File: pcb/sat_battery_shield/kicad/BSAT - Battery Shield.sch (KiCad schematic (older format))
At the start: 10 parts, among them P2 POWER, SW2 SAT POWER, U1 TP4056-MODULE, U2 TP4056-MODULE

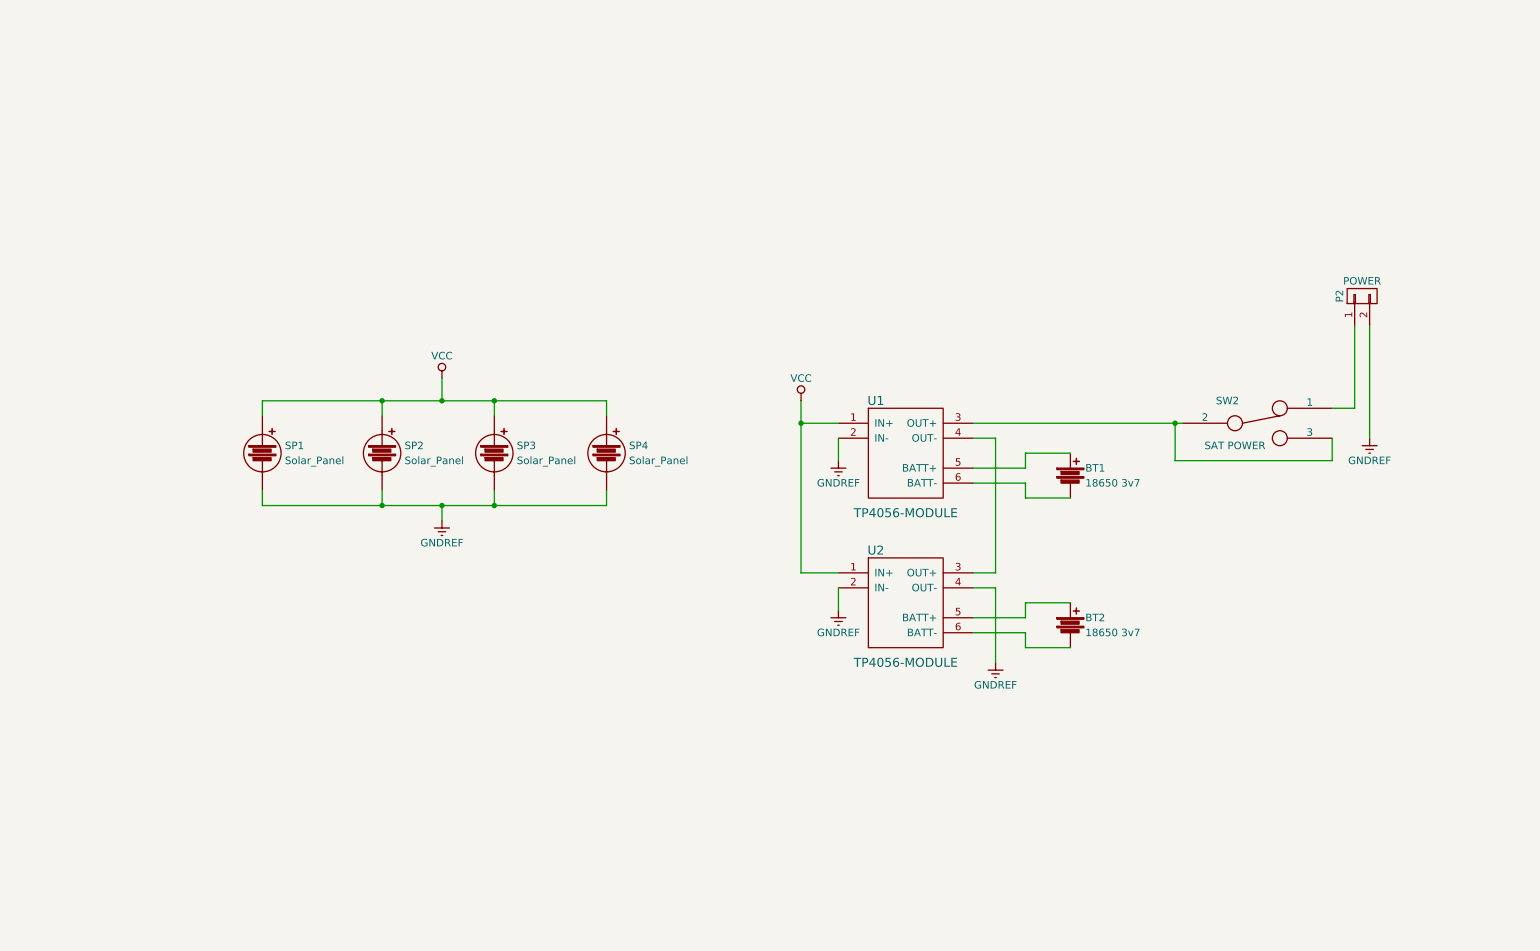
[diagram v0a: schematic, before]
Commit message: feat(battery-shield): Esquema reorganizado y optoacoplador añadido para el enable/disable del cargador.
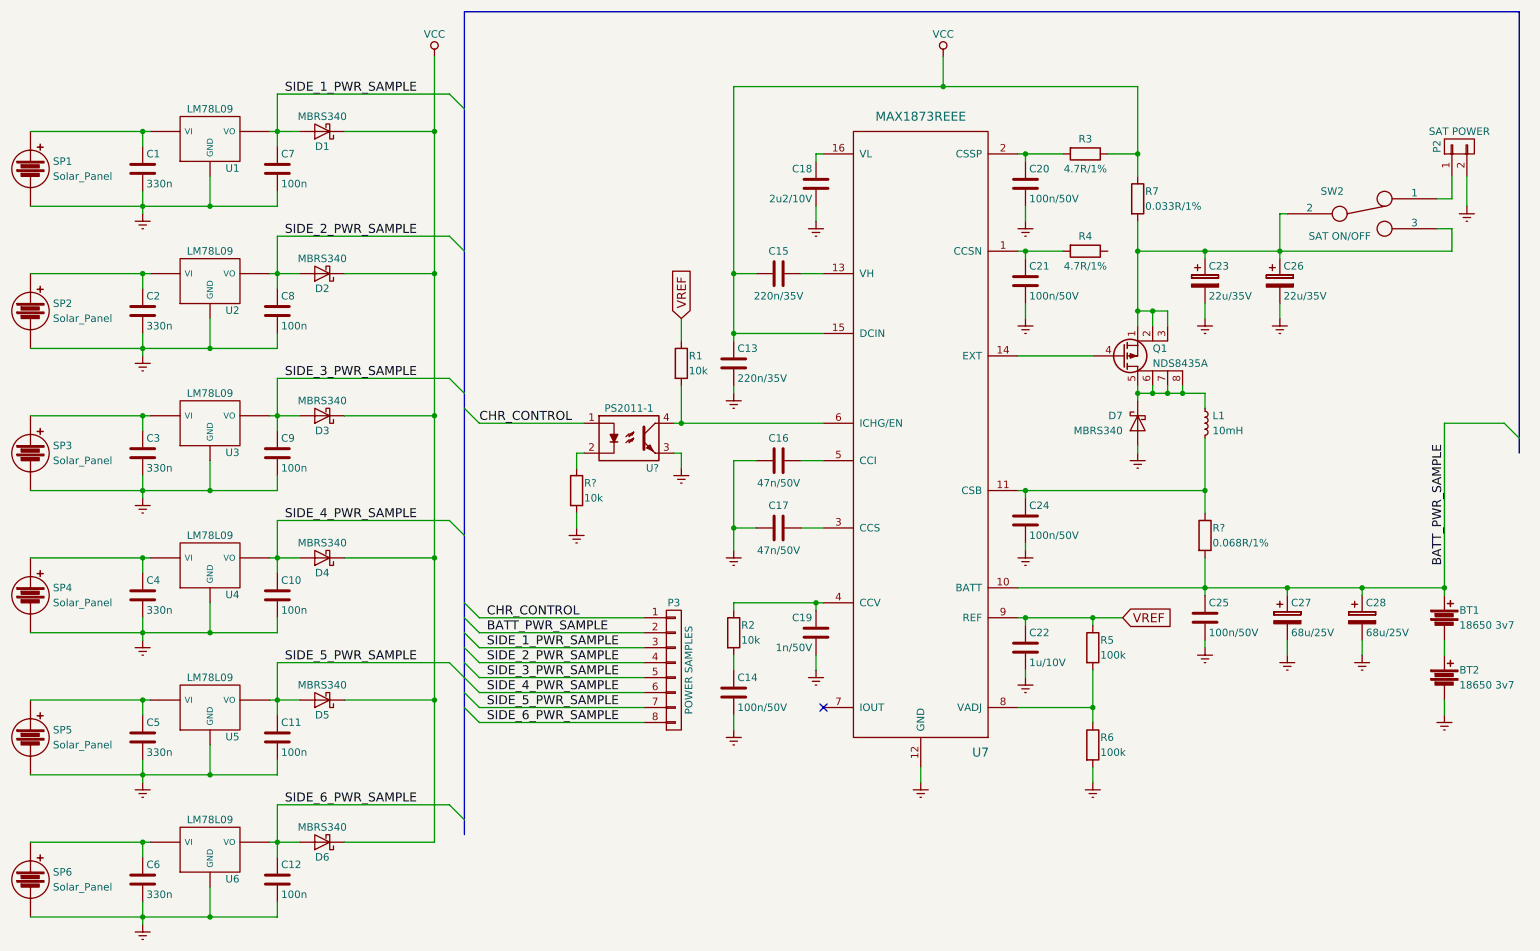
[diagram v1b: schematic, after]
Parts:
- removed U1, U2: TP4056-MODULE, BoscoverySAT:TP4056-MODULE, symbol TP4056-MODULE
- added C1, C2, C3, C4, C5, C6: 330n, symbol C
- added C10, C11, C12, C7, C8, C9: 100n, symbol C
- added C13, C15: 220n/35V, symbol C
- added C14, C20, C21, C24, C25: 100n/50V, symbol C
- added C16, C17: 47n/50V, symbol C
- added C18: 2u2/10V, symbol C
- added C19: 1n/50V, symbol C
- added C22: 1u/10V, symbol C
- added C23, C26: 22u/35V, symbol CP
- added C27, C28: 68u/25V, symbol CP
- added D1, D2, D3, D4, D5, D6, D7: MBRS340, symbol D_Schottky
- added L1: 10mH, symbol L_Small
- added P3: POWER SAMPLES, symbol CONN_01X08
- added Q1: NDS8435A, symbol NDS8435A
- added R1, R2, R?: 10k, symbol R
- added R3, R4: 4.7R/1%, symbol R
- added R5, R6: 100k, symbol R
- added R7: 0.033R/1%, symbol R
- added R?: 0.068R/1%, symbol R
- added SP5, SP6: Solar_Panel, Pin_Headers:Pin_Header_Straight_1x02, symbol Solar_Panel
- added U1, U2, U3, U4, U5, U6: LM78L09, symbol LM78L09
- added U7: MAX1873REEE, symbol MAX1873REEE
- added U?: PS2011-1, symbol PS2011-1
- P2: value POWER -> SAT POWER
- SW2: value SAT POWER -> SAT ON/OFF
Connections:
- net GNDREF: now also BT2.2, C1.2, C10.2, C11.2, C12.2, C13.2, C14.2, C16.1, C17.1, C18.2, C19.2, C2.2, C20.2, C21.2, C22.2, C23.2, C24.2, C25.2, C26.2, C27.2, C28.2, C3.2, C4.2, C5.2, C6.2, C7.2, C8.2, C9.2, D7.2 (A), R6.2, R?.2, SP5.2, SP6.2, U1.GND, U2.GND, U3.GND, U4.GND, U5.GND, U6.GND, U7.12 (GND), U?.3
- net VCC: now also C13.1, C15.1, D1.1 (K), D2.1 (K), D3.1 (K), D4.1 (K), D5.1 (K), D6.1 (K), R3.1, R7.1, U7.15 (DCIN); no longer SP1.1, SP2.1, SP3.1, SP4.1
- net at SW2.2, SW2.3: now also C23.1, C26.1, Q1.1 (S), Q1.2 (S), Q1.3 (S), R7.2
- net BATT_PWR_SAMPLE: now reaches BT1.1
- net BATT_PWR_SAMPLE: now also C25.1, C27.1, C28.1, P3.2 (P2), R?.2, U7.10 (BATT)
- net at BT1.2: now also BT2.1
- new net: C1.1, SP1.1, U1.VI
- new net: C21.1, R4.2, U7.1 (CCSN)
- new net: C24.1, L1.2, R?.1, U7.11 (CSB)
- new net: C15.2, U7.13 (VH)
- new net: Q1.4 (G), U7.14 (EXT)
- new net: C18.1, U7.16 (VL)
- new net: C20.1, R3.2, U7.2 (CSSP)
- new net: C17.2, U7.3 (CCS)
- new net: C19.1, R2.1, U7.4 (CCV)
- new net: C16.2, U7.5 (CCI)
- new net: R1.2, U7.6 (ICHG/EN), U?.4
- new net: R5.2, R6.1, U7.8 (VADJ)
- new net: C2.1, SP2.1, U2.VI
- new net: C3.1, SP3.1, U3.VI
- new net: C4.1, SP4.1, U4.VI
- new net: C5.1, SP5.1, U5.VI
- new net: C6.1, SP6.1, U6.VI
- new net: C14.1, R2.2
- new net: D7.1 (K), L1.1, Q1.5 (D), Q1.6 (D), Q1.7 (D), Q1.8 (D)
- new net: R?.1, U?.2
- new net CHR_CONTROL: P3.1 (P1), U?.1
- new net SIDE_1_PWR_SAMPLE: C7.1, D1.2 (A), P3.3 (P3), U1.VO
- new net SIDE_2_PWR_SAMPLE: C8.1, D2.2 (A), P3.4 (P4), U2.VO
- new net SIDE_3_PWR_SAMPLE: C9.1, D3.2 (A), P3.5 (P5), U3.VO
- new net SIDE_4_PWR_SAMPLE: C10.1, D4.2 (A), P3.6 (P6), U4.VO
- new net SIDE_5_PWR_SAMPLE: C11.1, D5.2 (A), P3.7 (P7), U5.VO
- new net SIDE_6_PWR_SAMPLE: C12.1, D6.2 (A), P3.8 (P8), U6.VO
- new net VREF: C22.1, R1.1, R5.1, U7.9 (REF)
- no-connect marks 0 -> 1
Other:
- moved on the sheet: BT1, BT2, P2, SP1, SW2

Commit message: refactor(battery-shield): Rediseño de la placa empleando el regulador de carga MAX1873.
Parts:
- BT1, BT2: symbol Battery -> Battery-RESCUE-BSAT_-_Battery_Shield
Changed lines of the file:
@@
 EESchema Schematic File Version 2
+LIBS:BSAT - Battery Shield-rescue
 LIBS:boscoverysat
 LIBS:power
@@
 $EndDescr
 $Comp
-L Battery BT1
+L Battery-RESCUE-BSAT_-_Battery_Shield BT1
 U 1 1 574296C6
 P 10200 4650
@@
 $EndComp
 $Comp
-L Battery BT2
+L Battery-RESCUE-BSAT_-_Battery_Shield BT2
 U 1 1 5745DC06
 P 10200 5050
@@
 56 56 50 5E 5E FE 2B 80 B2 AA AA AA 5F F3 F2 F2 AA 94 B7 F8 C7 44 5E 5E 9E D2 E3 4A 89 E4 4F FC
 09 79 74 C5 E6 42 7F E2 FF 19 FE 24 92 3F D1 26 FE 24 92 3F D1 26 FE 24 92 3F D1 26 FE 0F 78 6D
-04 45 FC BA DA 0A 00 00 00 00 49 45 4E 44 AE 42 60 82 38
+04 45 FC BA DA 0A 00 00 00 00 49 45 4E 44 AE 42 60 82
 EndData
 $EndBitmap
